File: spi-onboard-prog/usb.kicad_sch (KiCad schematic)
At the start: 13 parts, among them J3 USB_C_Receptacle_USB2.0_16P, Q3 12MHz, U2 CH341A

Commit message: layout work on onboard spi prog
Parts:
- removed C151, C152: 47u, Capacitor_SMD:C_1206_3216Metric_Pad1.33x1.80mm_HandSolder, symbol micropet_v3-eagle-import:CPOL-EUE5-6
- added C6: 47u, Capacitor_SMD:C_1206_3216Metric, symbol Device:C_Polarized
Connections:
- net GND: now also C6.2
- net at U2.9 (V3): now also C6.1
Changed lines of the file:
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@@
-		(color 0 0 0 0)
-	)
-	(junction
-		(at 122.555 163.195)
-		(diameter 0)
-		(color 0 0 0 0)
-	)
-	(junction
-		(at 122.555 144.78)
-		(diameter 0)
 		(color 0 0 0 0)
 	)
@@
 	(wire
 		(pts
-			(xy 122.555 160.655) (xy 122.555 163.195)
-		)
-		(stroke
-			(width 0)
-			(type default)
-		)
-	)
-	(wire
-		(pts
 			(xy 62.23 178.435) (xy 62.23 180.975)
-		)
-		(stroke
-			(width 0)
-			(type default)
-		)
-	)
-	(wire
-		(pts
-			(xy 122.555 144.78) (xy 122.555 153.035)
 		)
 		(stroke
@@
 	(wire
 		(pts
-			(xy 122.555 163.195) (xy 122.555 163.83)
-		)
-		(stroke
-			(width 0)
-			(type default)
-		)
-	)
-	(wire
-		(pts
 			(xy 116.205 163.195) (xy 112.395 163.195)
 		)
@@
 	(wire
 		(pts
-			(xy 130.81 144.78) (xy 122.555 144.78)
-		)
-		(stroke
-			(width 0)
-			(type default)
-		)
-	)
-	(wire
-		(pts
 			(xy 162.56 86.995) (xy 177.165 86.995)
 		)
@@
 	(wire
 		(pts
-			(xy 122.555 163.195) (xy 116.205 163.195)
-		)
-		(stroke
-			(width 0)
-			(type default)
-		)
-	)
-	(wire
-		(pts
 			(xy 77.47 155.575) (xy 82.55 155.575)
 		)
@@
 	(wire
 		(pts
-			(xy 77.47 140.335) (xy 122.555 140.335)
+			(xy 77.47 140.335) (xy 114.935 140.335)
 		)
 		(stroke
@@
 	(wire
 		(pts
-			(xy 122.555 140.335) (xy 122.555 144.78)
-		)
-		(stroke
-			(width 0)
-			(type default)
-		)
-	)
-	(wire
-		(pts
 			(xy 121.92 120.65) (xy 121.92 97.155)
 		)
@@
 	(global_label "VCCIN"
 		(shape input)
-		(at 130.81 144.78 0)
+		(at 114.935 140.335 0)
 		(fields_autoplaced yes)
 		(effects
@@
 		)
 		(property "Intersheetrefs" "${INTERSHEET_REFS}"
-			(at 139.3591 144.78 0)
+			(at 123.4841 140.335 0)
 			(hide yes)
 			(show_name no)
@@
 				(path "/d4f435f9-695d-422f-9894-15a20b29134d"
 					(reference "R11")
-					(unit 1)
-				)
-			)
-		)
-	)
-	(symbol
-		(lib_id "micropet_v3-eagle-import:CPOL-EUE5-6")
-		(at 122.555 155.575 0)
-		(unit 1)
-		(body_style 1)
-		(exclude_from_sim no)
-		(in_bom yes)
-		(on_board yes)
-		(in_pos_files yes)
-		(dnp no)
-		(property "Reference" "C151"
-			(at 123.698 155.0924 0)
-			(show_name no)
-			(do_not_autoplace no)
-			(effects
-				(font
-					(size 1.778 1.5113)
-				)
-				(justify left bottom)
-			)
-		)
-		(property "Value" "47u"
-			(at 123.698 160.1724 0)
-			(show_name no)
-			(do_not_autoplace no)
-			(effects
-				(font
-					(size 1.778 1.5113)
-				)
-				(justify left bottom)
-			)
-		)
-		(property "Footprint" "Capacitor_SMD:C_1206_3216Metric_Pad1.33x1.80mm_HandSolder"
-			(at 122.555 155.575 0)
-			(hide yes)
-			(show_name no)
-			(do_not_autoplace no)
-			(effects
-				(font
-					(size 1.27 1.27)
-				)
-			)
-		)
-		(property "Datasheet" ""
-			(at 122.555 155.575 0)
-			(hide yes)
-			(show_name no)
-			(do_not_autoplace no)
-			(effects
-				(font
-					(size 1.27 1.27)
-				)
-			)
-		)
-		(property "Description" ""
-			(at 122.555 155.575 0)
-			(hide yes)
-			(show_name no)
-			(do_not_autoplace no)
-			(effects
-				(font
-					(size 1.27 1.27)
-				)
-			)
-		)
-		(pin "+"
-		)
-		(pin "-"
-		)
-		(instances
-			(project "spi-onboard-prog"
-				(path "/d4f435f9-695d-422f-9894-15a20b29134d"
-					(reference "C151")
 					(unit 1)
 				)
@@
 	)
 	(symbol
-		(lib_id "micropet_v3-eagle-import:CPOL-EUE5-6")
-		(at 153.67 48.895 0)
+		(lib_id "Device:C_Polarized")
+		(at 153.67 50.165 0)
 		(unit 1)
 		(body_style 1)
@@
 		(in_pos_files yes)
 		(dnp no)
-		(property "Reference" "C152"
-			(at 154.813 48.4124 0)
-			(show_name no)
-			(do_not_autoplace no)
-			(effects
-				(font
-					(size 1.778 1.5113)
-				)
-				(justify left bottom)
+		(fields_autoplaced yes)
+		(property "Reference" "C6"
+			(at 156.845 48.0059 0)
+			(show_name no)
+			(do_not_autoplace no)
+			(effects
+				(font
+					(size 1.27 1.27)
+				)
+				(justify left)
 			)
 		)
 		(property "Value" "47u"
-			(at 154.813 53.4924 0)
-			(show_name no)
-			(do_not_autoplace no)
-			(effects
-				(font
-					(size 1.778 1.5113)
-				)
-				(justify left bottom)
-			)
-		)
-		(property "Footprint" "Capacitor_SMD:C_1206_3216Metric_Pad1.33x1.80mm_HandSolder"
-			(at 153.67 48.895 0)
+			(at 156.845 50.5459 0)
+			(show_name no)
+			(do_not_autoplace no)
+			(effects
+				(font
+					(size 1.27 1.27)
+				)
+				(justify left)
+			)
+		)
+		(property "Footprint" "Capacitor_SMD:C_1206_3216Metric"
+			(at 154.6352 53.975 0)
 			(hide yes)
 			(show_name no)
@@
 		)
 		(property "Datasheet" ""
-			(at 153.67 48.895 0)
-			(hide yes)
-			(show_name no)
-			(do_not_autoplace no)
-			(effects
-				(font
-					(size 1.27 1.27)
-				)
-			)
-		)
-		(property "Description" ""
-			(at 153.67 48.895 0)
-			(hide yes)
-			(show_name no)
-			(do_not_autoplace no)
-			(effects
-				(font
-					(size 1.27 1.27)
-				)
-			)
-		)
-		(pin "+"
-		)
-		(pin "-"
+			(at 153.67 50.165 0)
+			(hide yes)
+			(show_name no)
+			(do_not_autoplace no)
+			(effects
+				(font
+					(size 1.27 1.27)
+				)
+			)
+		)
+		(property "Description" "Polarized capacitor"
+			(at 153.67 50.165 0)
+			(hide yes)
+			(show_name no)
+			(do_not_autoplace no)
+			(effects
+				(font
+					(size 1.27 1.27)
+				)
+			)
+		)
+		(pin "2"
+		)
+		(pin "1"
 		)
 		(instances
 			(project "spi-onboard-prog"
 				(path "/d4f435f9-695d-422f-9894-15a20b29134d"
-					(reference "C152")
+					(reference "C6")
 					(unit 1)
 				)

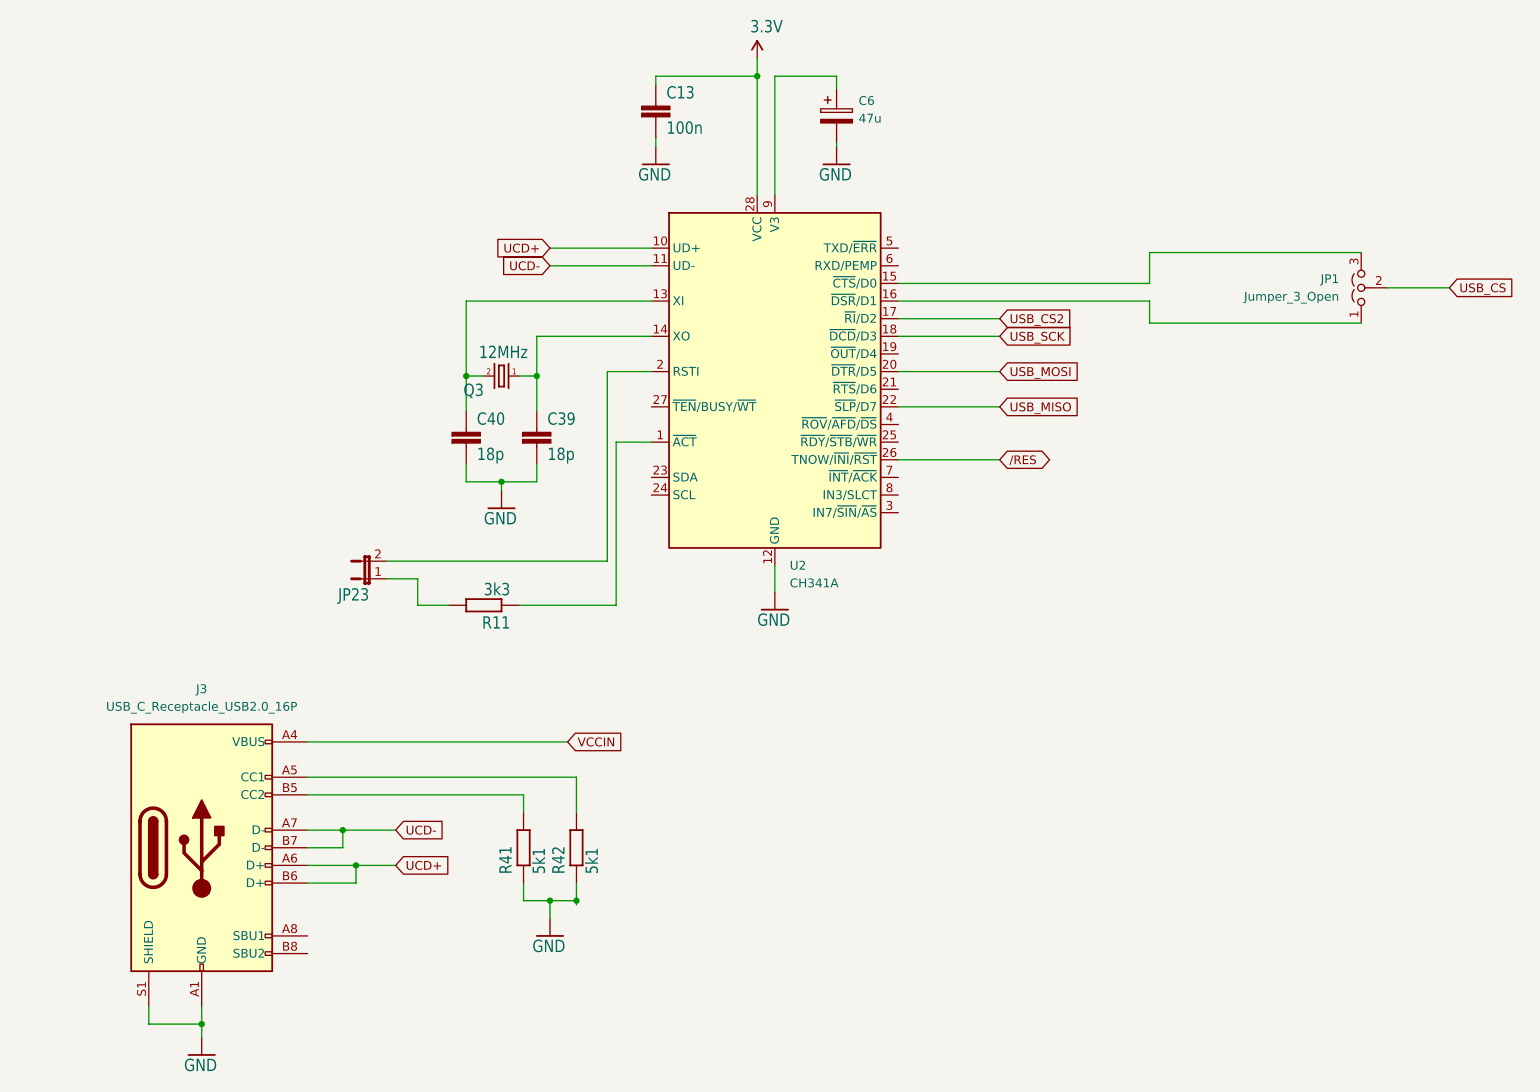
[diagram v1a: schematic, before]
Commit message: onboard prog on SPI10-3.3V
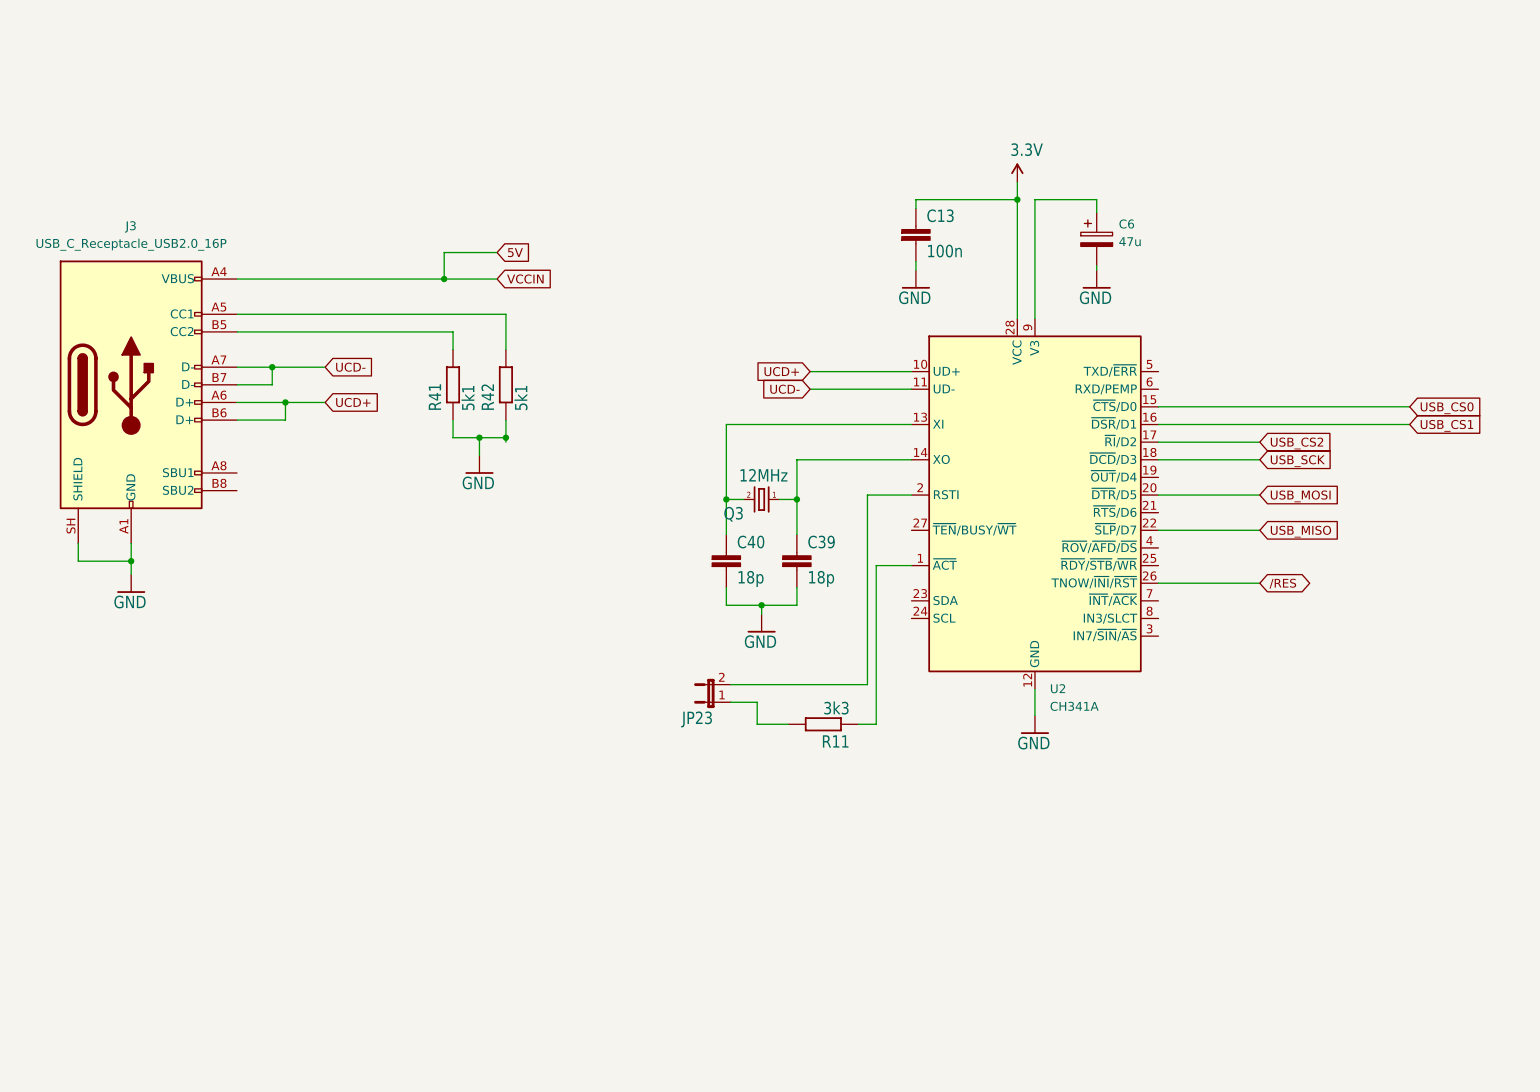
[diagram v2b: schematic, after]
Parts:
- removed JP1: Jumper_3_Open, Connector_PinHeader_2.54mm:PinHeader_1x03_P2.54mm_Vertical, symbol Jumper:Jumper_3_Open
- Q3: LCSC (none) -> C16369
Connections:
- net GND: now also J3.SH (SHIELD); no longer J3.S1 (SHIELD)
- net USB_CS0: now reaches U2.15 (~{CTS}/D0)
- net USB_CS1: now reaches U2.16 (~{DSR}/D1)
- net VCCIN renamed 5V
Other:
- moved on the sheet: C13, C39, C40, C6, J3, JP23, Q3, R11, R41, R42, U2

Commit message: onboard flash prog
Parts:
- added U6: 74LVC1G04, Package_TO_SOT_SMD:SOT-23-5_HandSoldering, symbol 74xGxx:74LVC1G04
- U2: footprint Package_SO:SOIC-28W_7.5x17.9mm_P1.27mm -> Package_SO:SOP-28_8.4x18.16mm_P1.27mm
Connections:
- net 3.3V: now also C6.1, U2.9 (V3), U6.5 (VCC)
- net GND: now also U6.3 (GND)
- net at U2.2 (RSTI): now also U6.4; no longer JP23.2
- net /RES: no longer names the net of U2.26 (TNOW/~{INI}/~{RST})
- net /RES: now also JP23.2
- new net /RES: U6.2
